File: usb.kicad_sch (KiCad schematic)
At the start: 10 parts, among them J2 USB_C_Receptacle_USB2.0

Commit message: Minor improvements
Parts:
- removed D3: D, Diode_SMD:D_0603_1608Metric, symbol Device:D
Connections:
- net VBUS: now also F1.2
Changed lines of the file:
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@@
 	(wire
 		(pts
-			(xy 127 81.28) (xy 130.81 81.28)
+			(xy 127 81.28) (xy 142.24 81.28)
 		)
 		(stroke
@@
 		(pts
 			(xy 96.52 127) (xy 100.33 127)
-		)
-		(stroke
-			(width 0)
-			(type default)
-		)
-	)
-	(wire
-		(pts
-			(xy 138.43 81.28) (xy 142.24 81.28)
 		)
 		(stroke
@@
 					(unit 1)
 				)
-			)
-		)
-	)
-	(symbol
-		(lib_id "Device:D")
-		(at 134.62 81.28 180)
-		(unit 1)
-		(exclude_from_sim no)
-		(in_bom yes)
-		(on_board yes)
-		(dnp no)
-		(fields_autoplaced yes)
-		(property "Reference" "D3"
-			(at 134.62 74.93 0)
-			(effects
-				(font
-					(size 1.27 1.27)
-				)
-			)
-		)
-		(property "Value" "D"
-			(at 134.62 77.47 0)
-			(effects
-				(font
-					(size 1.27 1.27)
-				)
-			)
-		)
-		(property "Footprint" "Diode_SMD:D_0603_1608Metric"
-			(at 134.62 81.28 0)
-			(effects
-				(font
-					(size 1.27 1.27)
-				)
-				(hide yes)
-			)
-		)
-		(property "Datasheet" "~"
-			(at 134.62 81.28 0)
-			(effects
-				(font
-					(size 1.27 1.27)
-				)
-				(hide yes)
-			)
-		)
-		(property "Description" "Diode"
-			(at 134.62 81.28 0)
-			(effects
-				(font
-					(size 1.27 1.27)
-				)
-				(hide yes)
-			)
-		)
-		(property "Sim.Device" "D"
-			(at 134.62 81.28 0)
-			(effects
-				(font
-					(size 1.27 1.27)
-				)
-				(hide yes)
-			)
-		)
-		(property "Sim.Pins" "1=K 2=A"
-			(at 134.62 81.28 0)
-			(effects
-				(font
-					(size 1.27 1.27)
-				)
-				(hide yes)
-			)
-		)
-		(pin "2"
-		)
-		(pin "1"
-		)
-		(instances
-			(project ""
-				(path "/7db990e4-92e1-4f99-b4d2-435bbec1ba83/00000000-0000-0000-0000-000061925999"
-					(reference "D3")
-					(unit 1)
-				)

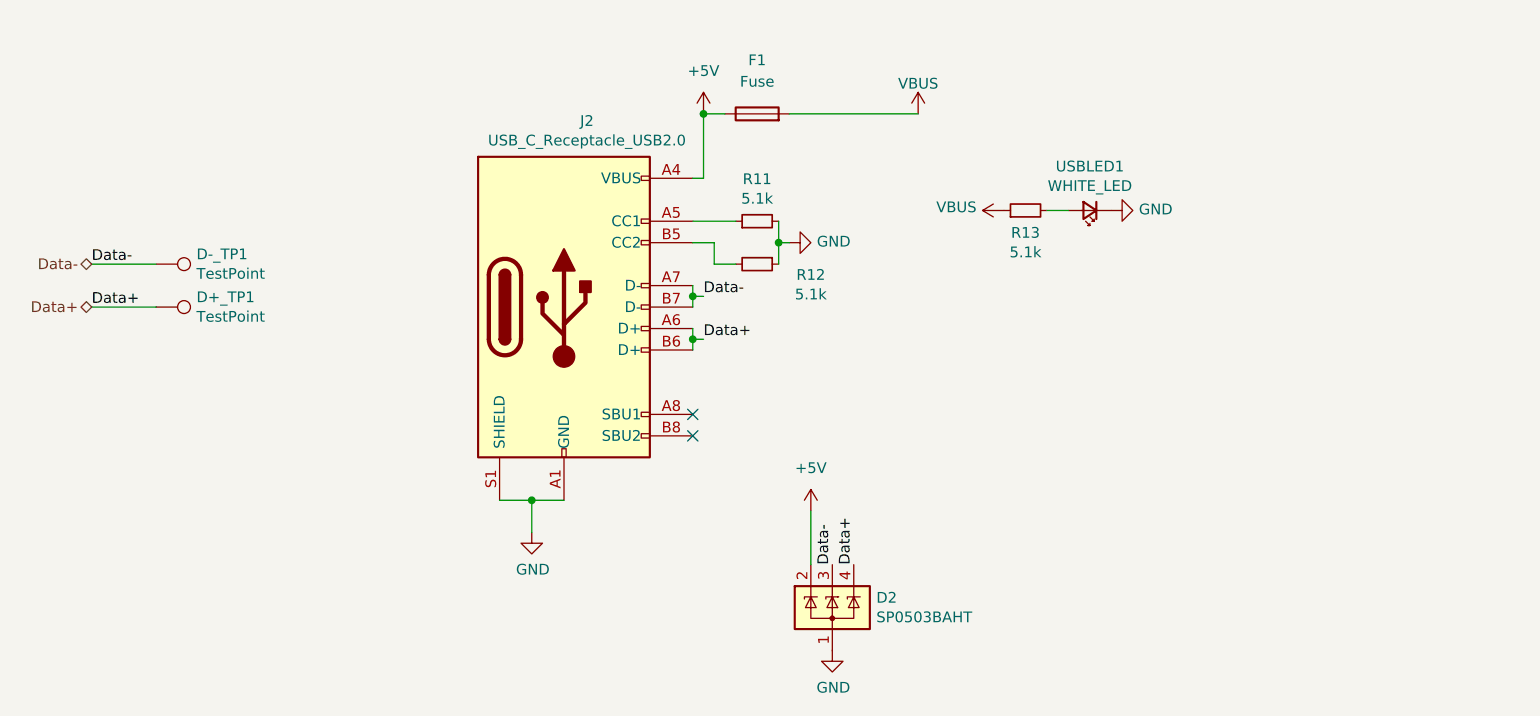
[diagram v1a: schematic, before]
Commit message: Fixed Libraries
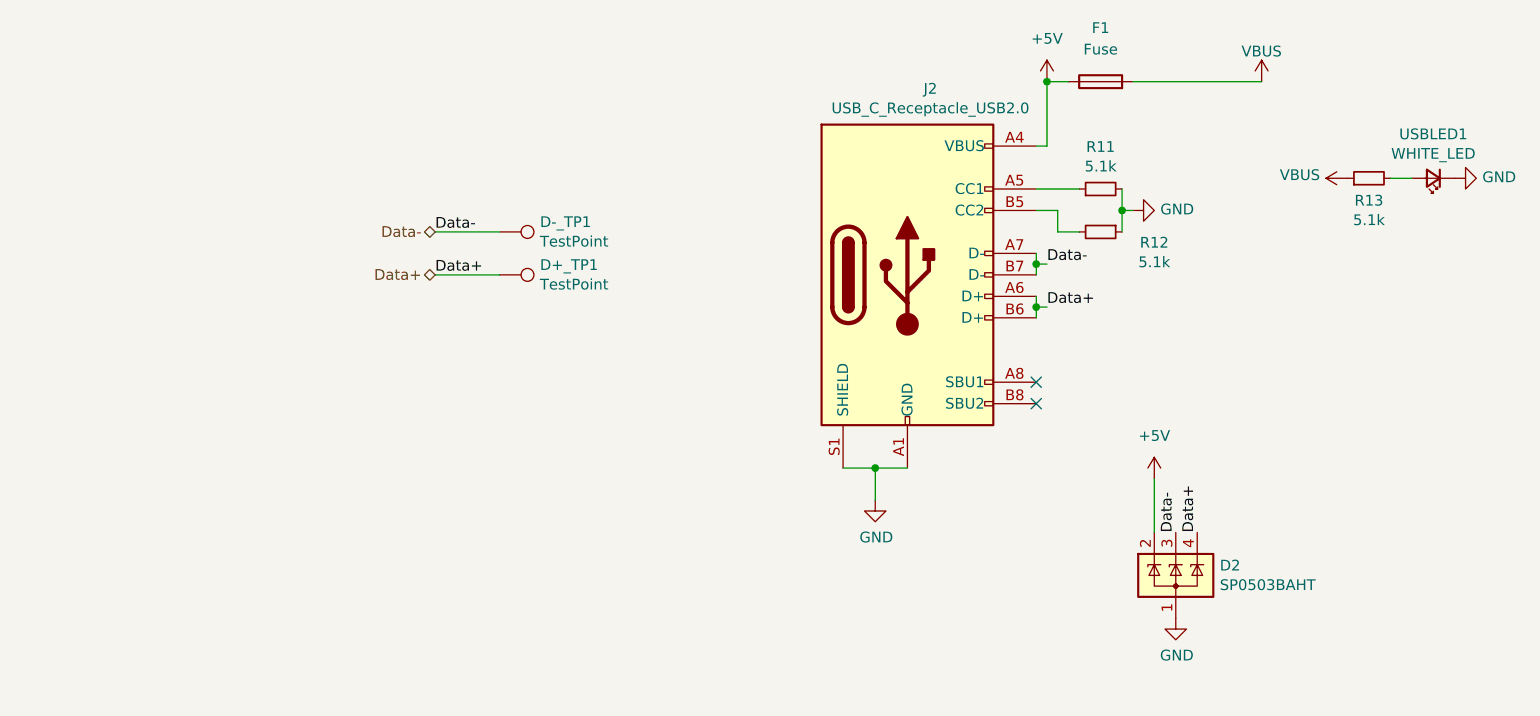
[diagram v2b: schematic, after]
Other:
- moved on the sheet: D+_TP1, D-_TP1, D2, F1, J2, R11, R12, R13, USBLED1

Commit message: Finishing touches without BOM
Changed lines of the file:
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@@
 (kicad_sch
-	(version 20231120)
+	(version 20250114)
 	(generator "eeschema")
-	(generator_version "8.0")
+	(generator_version "9.0")
 	(paper "A4")
 	(junction
@@
 	(label "Data+"
 		(at 175.26 130.81 90)
-		(fields_autoplaced yes)
 		(effects
 			(font
@@
 	(label "Data+"
 		(at 85.09 100.33 0)
-		(fields_autoplaced yes)
 		(effects
 			(font
@@
 	(label "Data-"
 		(at 85.09 95.25 0)
-		(fields_autoplaced yes)
 		(effects
 			(font
@@
 	(label "Data-"
 		(at 172.72 130.81 90)
-		(fields_autoplaced yes)
 		(effects
 			(font
@@
 	(label "Data-"
 		(at 157.48 99.06 0)
-		(fields_autoplaced yes)
 		(effects
 			(font
@@
 	(label "Data+"
 		(at 157.48 104.14 0)
-		(fields_autoplaced yes)
 		(effects
 			(font
@@
 		(shape bidirectional)
 		(at 85.09 95.25 180)
-		(fields_autoplaced yes)
 		(effects
 			(font
@@
 		(shape bidirectional)
 		(at 85.09 100.33 180)
-		(fields_autoplaced yes)
-		(effects
-			(font
+		(effects
+			(font

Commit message: finishing changes
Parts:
- USBLED1: footprint Resistor_SMD:R_0402_1005Metric -> Diode_SMD:D_0402_1005Metric
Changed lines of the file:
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@@
 			)
 		)
-		(property "Footprint" "Resistor_SMD:R_0402_1005Metric"
+		(property "Footprint" "Diode_SMD:D_0402_1005Metric"
 			(at 203.2 88.9 90)
 			(effects
